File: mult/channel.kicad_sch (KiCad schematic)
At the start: 15 parts, among them J2 Eurorack_Mono_Jack, J3 Eurorack_Mono_Jack, J4 Eurorack_Mono_Jack_No_S, J5 Eurorack_Mono_Jack_No_S, U1 OPA4197xPW

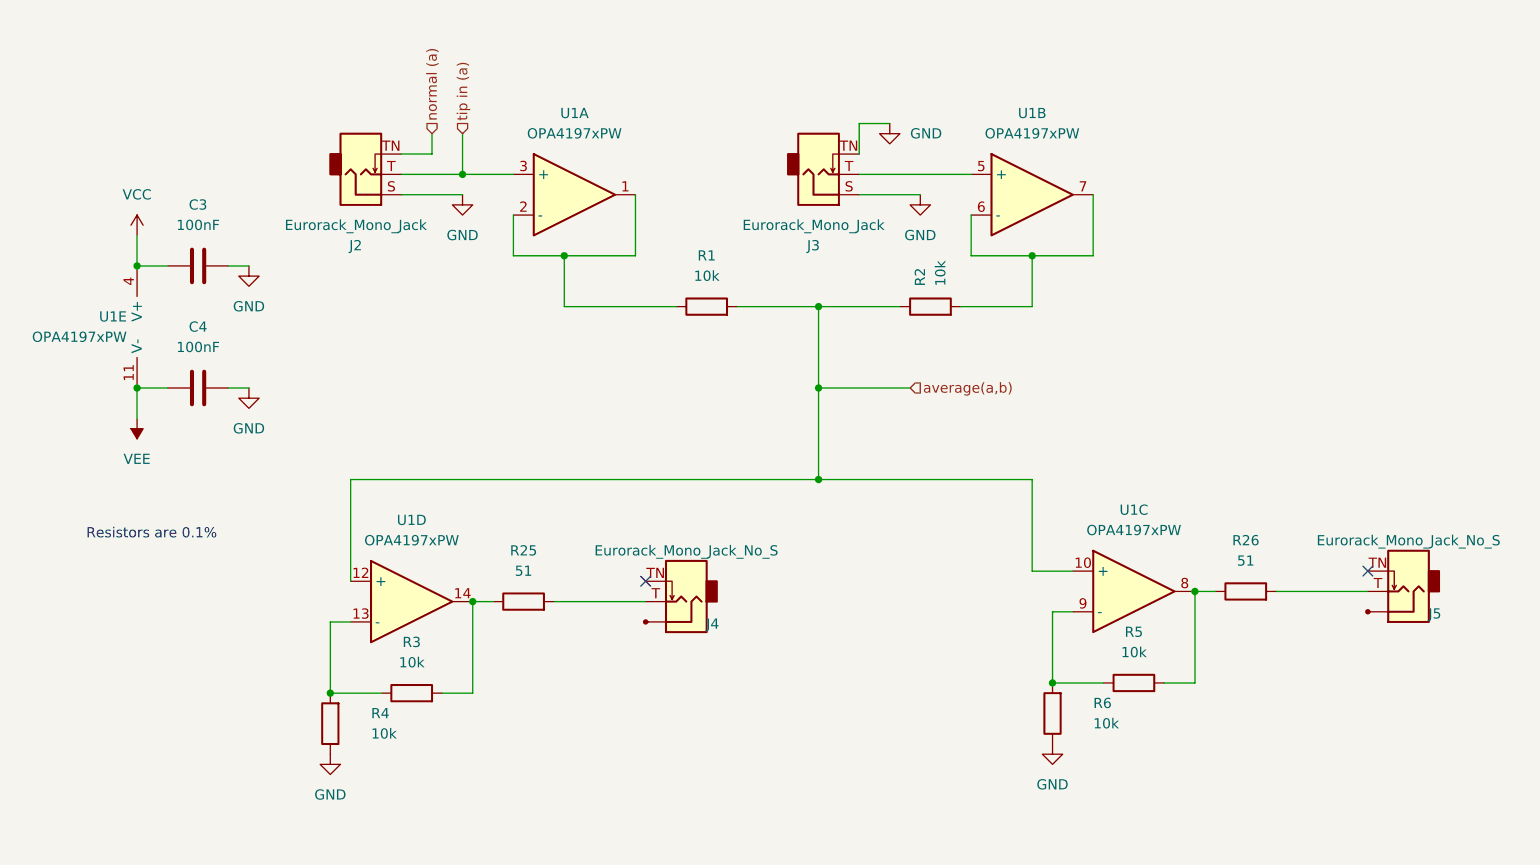
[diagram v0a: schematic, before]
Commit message: mult: Remove LEDs, add A-B output
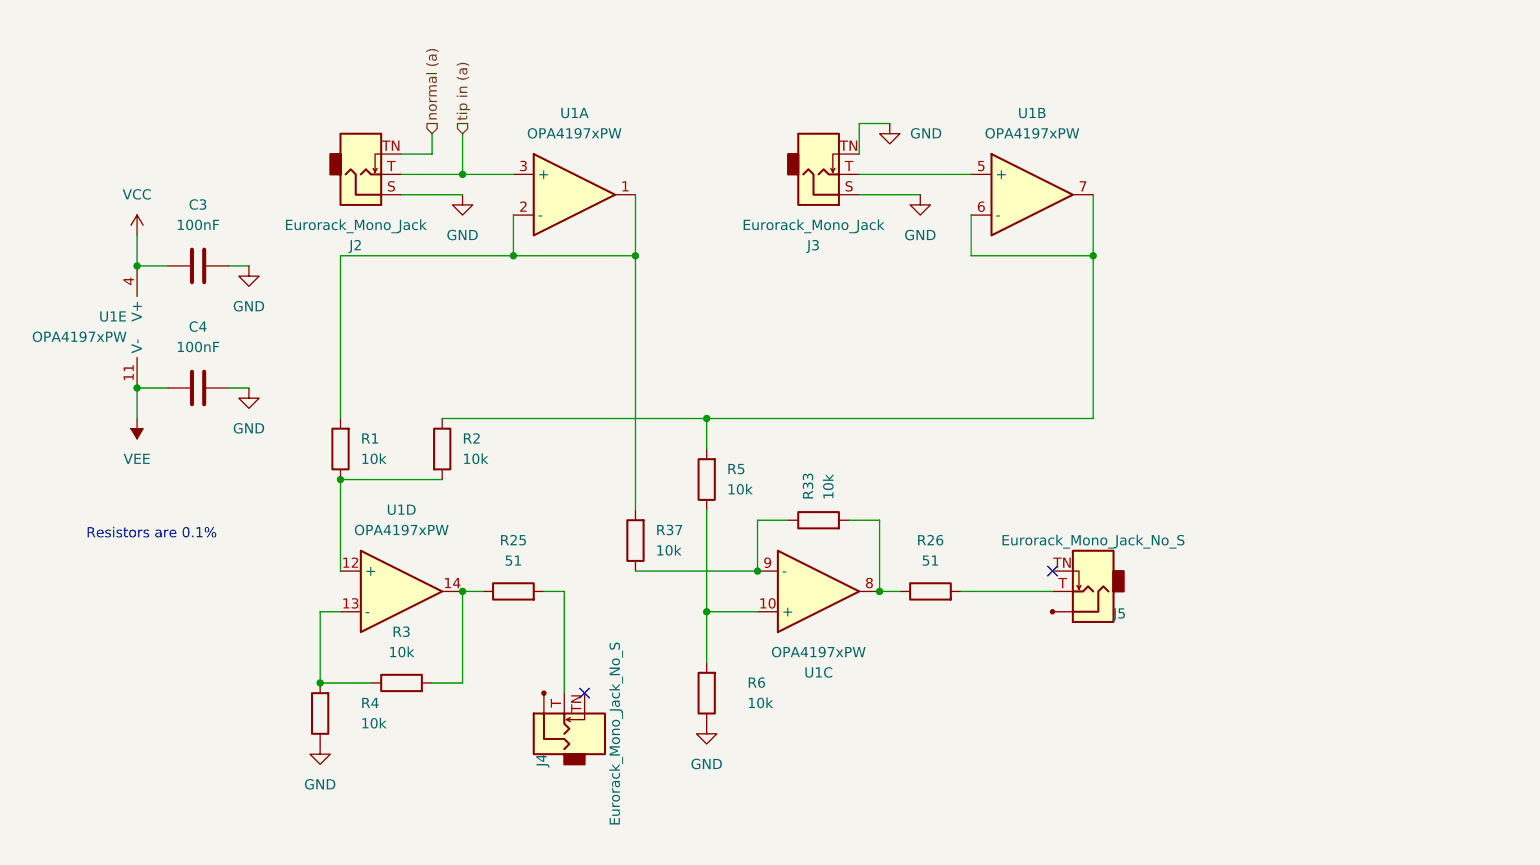
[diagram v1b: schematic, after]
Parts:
- added R33, R37: 10k, Resistor_SMD:R_0805_2012Metric_Pad1.20x1.40mm_HandSolder, symbol Device:R
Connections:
- net at U1.1, U1.2 (-): now also R1.2, R37.2; no longer R1.1
- net at U1.6 (-), U1.7: now also R2.1, R5.2; no longer R2.2
- net at R26.1, U1.8: now also R33.2; no longer R5.2
- net at R5.1, R6.2: now also U1.10 (+); no longer U1.9 (-)
- removed net average(a,b): R1.2, R2.1, U1.10 (+), U1.12 (+)
- new net: R1.1, R2.2, U1.12 (+)
- new net: R33.1, R37.1, U1.9 (-)
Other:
- moved on the sheet: J4, J5, R1, R2, R25, R26, R3, R4, R5, R6, U1C, U1D

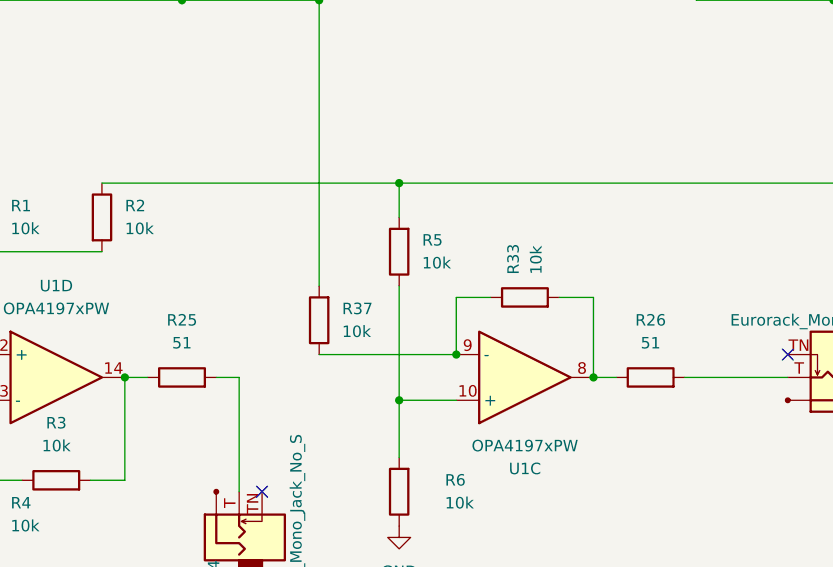
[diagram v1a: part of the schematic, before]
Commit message: mult: Update resistor references
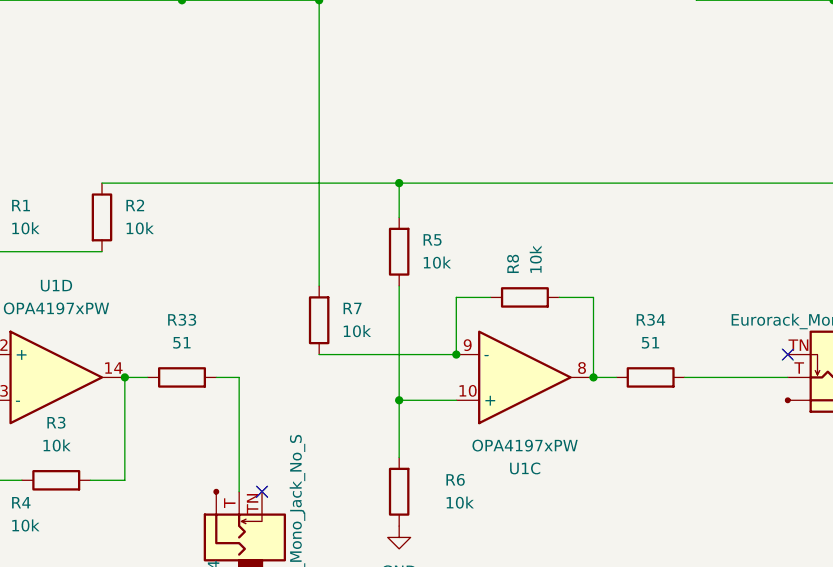
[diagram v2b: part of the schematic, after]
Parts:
- renumbered R25 to R33, R26 to R34, R37 to R7, R33 to R8

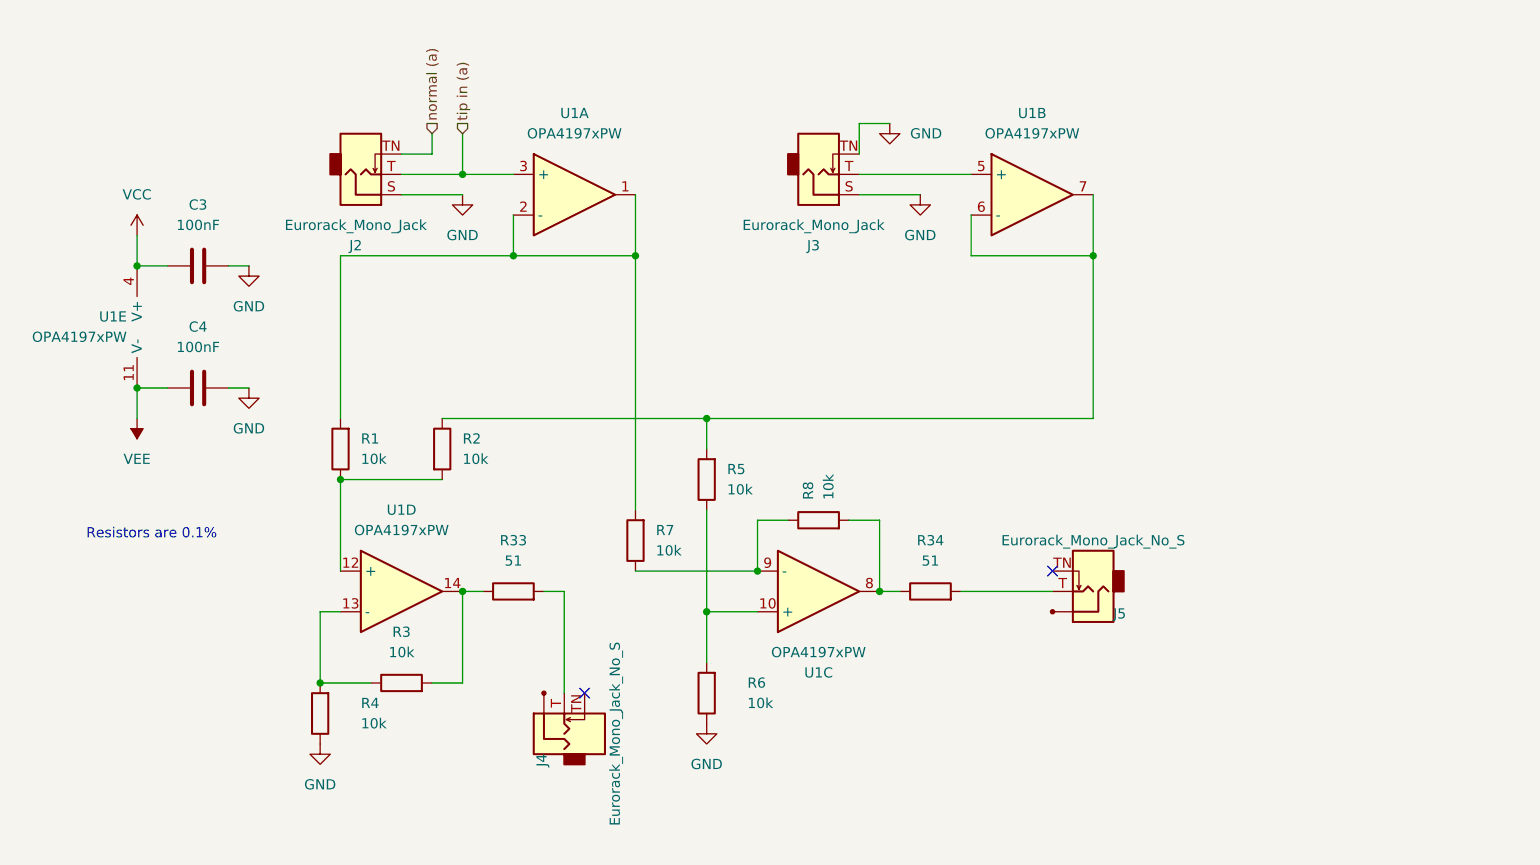
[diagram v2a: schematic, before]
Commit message: mult: Initial board routed, all items connected
Still expecting to make major changes this looks like mostly-random item
placements.
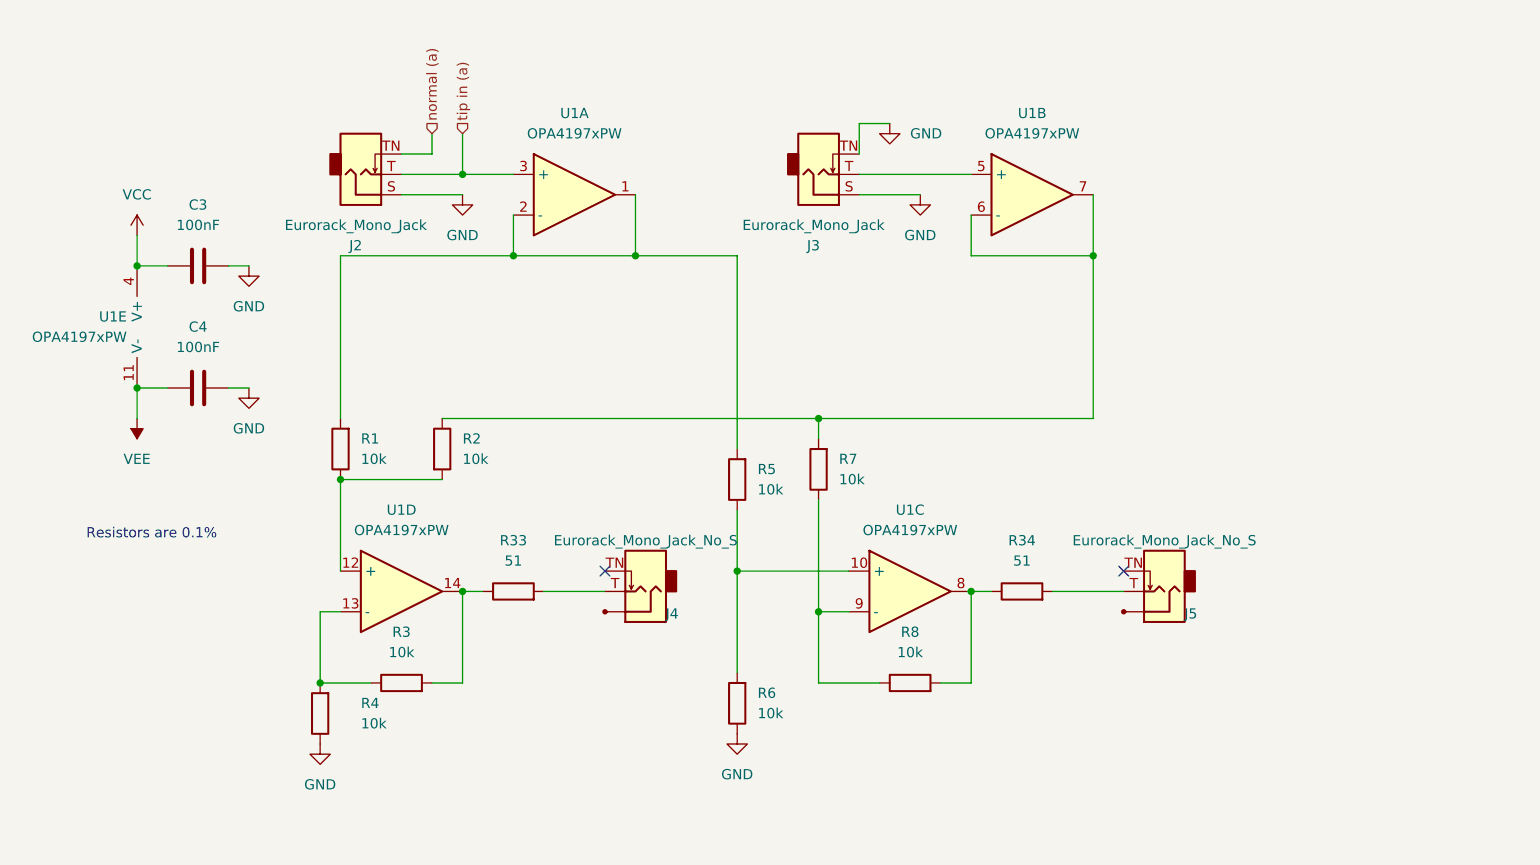
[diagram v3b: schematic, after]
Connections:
- net at R1.2, U1.1, U1.2 (-): now also R5.2; no longer R7.2
- net at R2.1, U1.6 (-), U1.7: now also R7.2; no longer R5.2
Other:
- moved on the sheet: J4, J5, R34, R5, R6, R7, R8, U1C

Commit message: mult: Replace OPA4917 with OPA1697
This seems reasonable performance (2mV offset max, audio op amp etc) and
significantly lower cost.
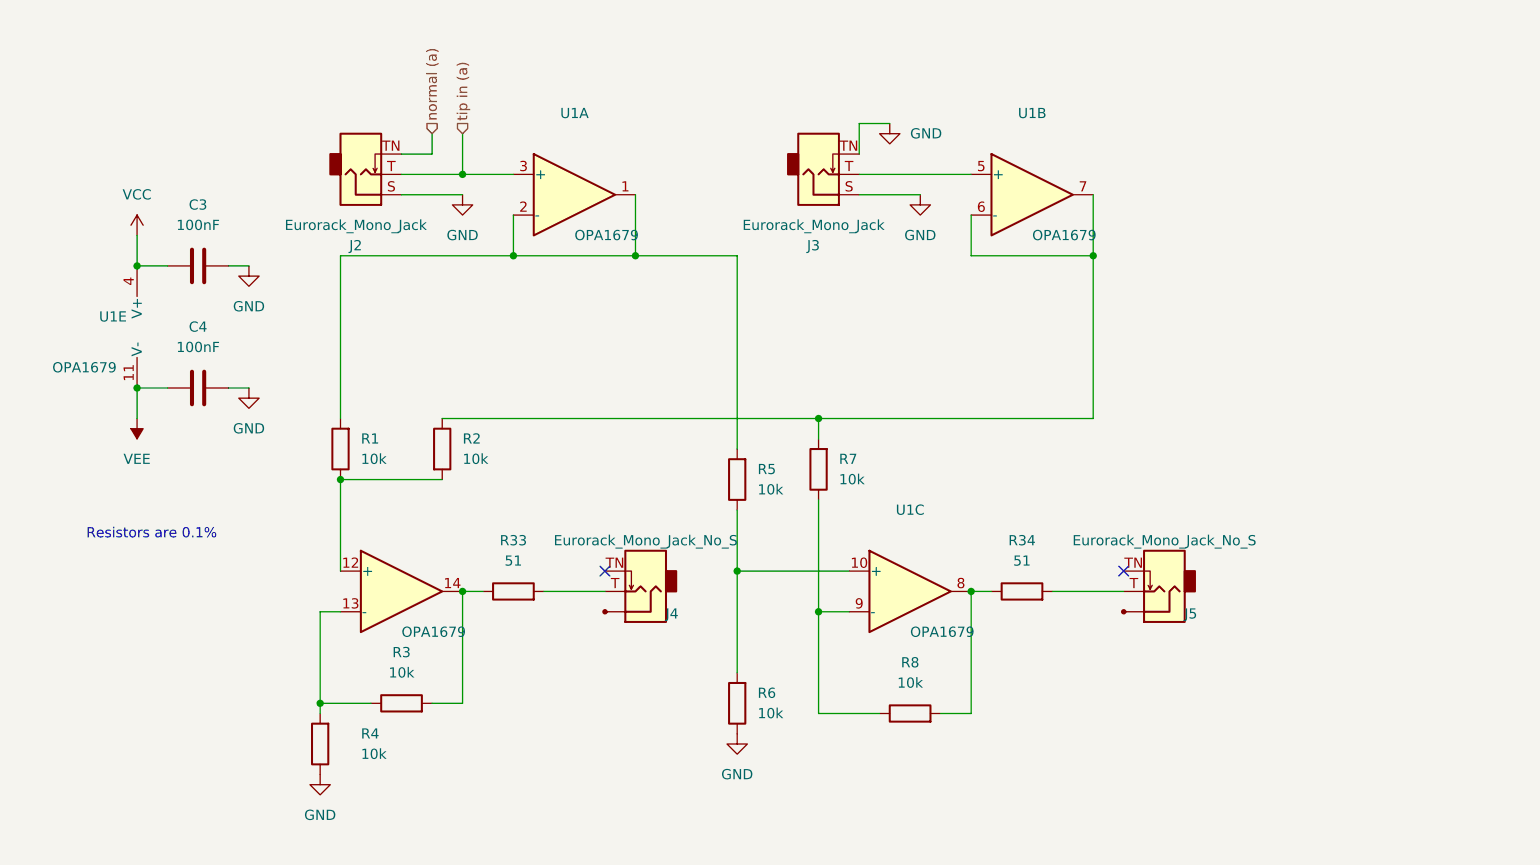
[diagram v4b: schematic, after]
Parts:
- U1: value OPA4197xPW -> OPA1679; symbol Amplifier_Operational:OPA4197xPW -> Amplifier_Operational:OPA1679
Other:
- moved on the sheet: R3, R4, R8

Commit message: mult: Progress rerouting easier layout
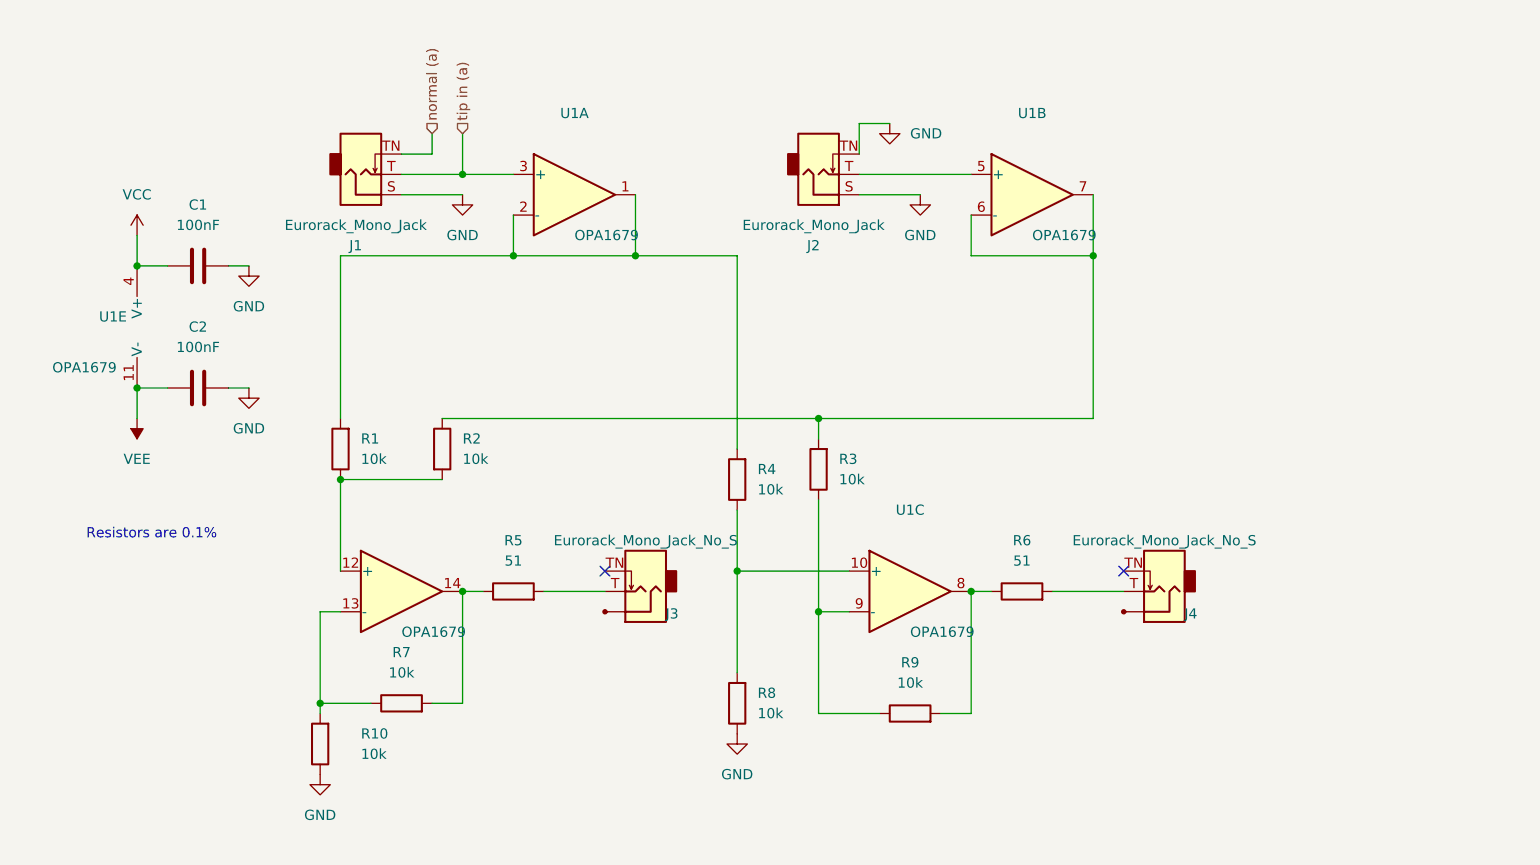
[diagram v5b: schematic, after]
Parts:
- renumbered C3 to C1, C4 to C2, J2 to J1, J3 to J2, J4 to J3, J5 to J4, R4 to R10, R7 to R3, R5 to R4, R33 to R5, R34 to R6, R3 to R7, R6 to R8, R8 to R9
